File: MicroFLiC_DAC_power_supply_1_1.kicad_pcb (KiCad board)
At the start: 2 copper layers, 49.8 x 49.8 mm, 61 parts, among them P1 Socket_1x2, P2 Header_1x2, P3 Socket_2x4, U1 AP1117D50, U2 AP1117, U3 AP1117, U4 LM317, U5 LM317

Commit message: Completed part descriptions
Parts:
- U1: value AP1117D50 -> AP1117E50
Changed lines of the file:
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@@
   )
   (setup
-    (last_trace_width 0.508)
+    (last_trace_width 0.254)
     (user_trace_width 0.381)
     (user_trace_width 0.508)
@@
       (effects (font (size 1 1) (thickness 0.15)))
     )
-    (fp_text value AP1117D50 (at 0 0.762 90) (layer F.Fab) hide
-      (effects (font (size 1 1) (thickness 0.15)))
-    )
+    (fp_text value AP1117E50 (at 0 0.762 90) (layer F.Fab) hide
+      (effects (font (size 1 1) (thickness 0.15)))
+    )

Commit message: Added feedback filtering capacitors and protection diodes
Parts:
- added C21: 10u/6.3V, Capacitors_SMD:C_0805, B.Cu at (123.5, 129.0)
- added C22: 10u/6.3V, Capacitors_SMD:C_0805, B.Cu at (121.7, 137.2)
- added C23: 10u/6.3V, Capacitors_SMD:C_0805, B.Cu at (119.4, 122.4)
- added C24: 10u/6.3V, Capacitors_SMD:C_0805, B.Cu at (115.1, 111.3)
- added D6: 1N4148, Diodes_SMD:SOD-323, B.Cu at (113.3, 116.6)
- added D7: 1N4148, Diodes_SMD:SOD-323, B.Cu at (111.8, 107.2)
- added D8: 1N4148, Diodes_SMD:SOD-323, B.Cu at (111.3, 118.6)
- added D9: 1N4148, Diodes_SMD:SOD-323, B.Cu at (111.8, 110.2)
- renumbered C21 to C25, C22 to C26, C23 to C27, C24 to C28, C25 to C29
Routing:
- net /FB_D: track 4.58 -> 11.8 mm, vias 1 -> 2
- net /19V_GND: track 95.9 -> 101.8 mm, vias 1 -> 2
- net /-7.5V: track 60.2 -> 65.0 mm
- net /FB_E: track 4.44 -> 8.65 mm, vias 1 -> 2
- net /+19V: track 41.8 -> 45.2 mm, vias 1 -> 2
- net /+24_IE: track 14.5 -> 17.0 mm, vias 0 -> 1
- net /-19V: track 75.0 -> 76.4 mm
- net /+24_ID: track 13.5 -> 14.7 mm, vias 0 -> 1
- net /FB_C: track 6.29 -> 7.25 mm
- net /FB_B: vias 0 -> 1
- net /7.5V_GND: vias 2 -> 3

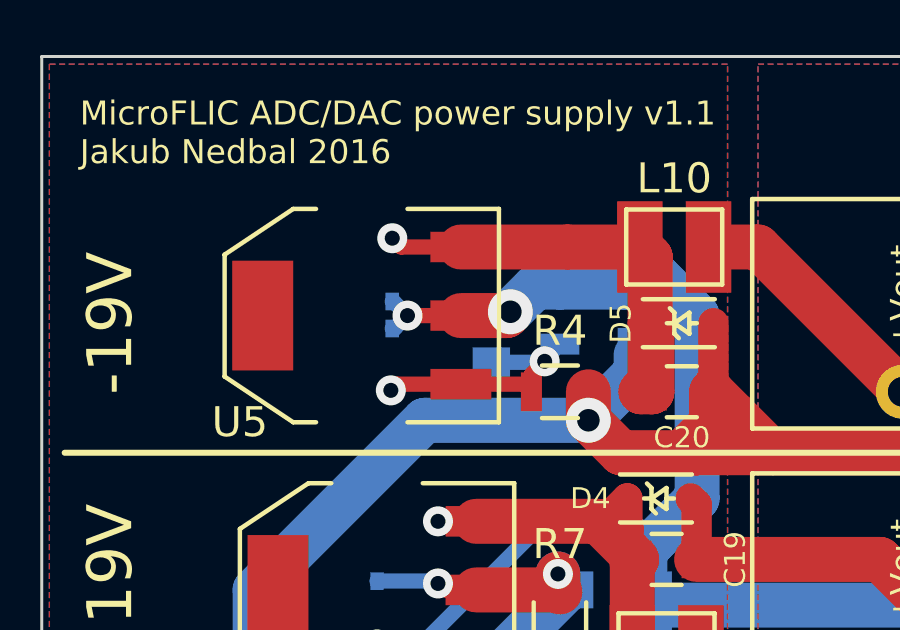
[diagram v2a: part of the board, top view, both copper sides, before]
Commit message: Fixed capacitor order code
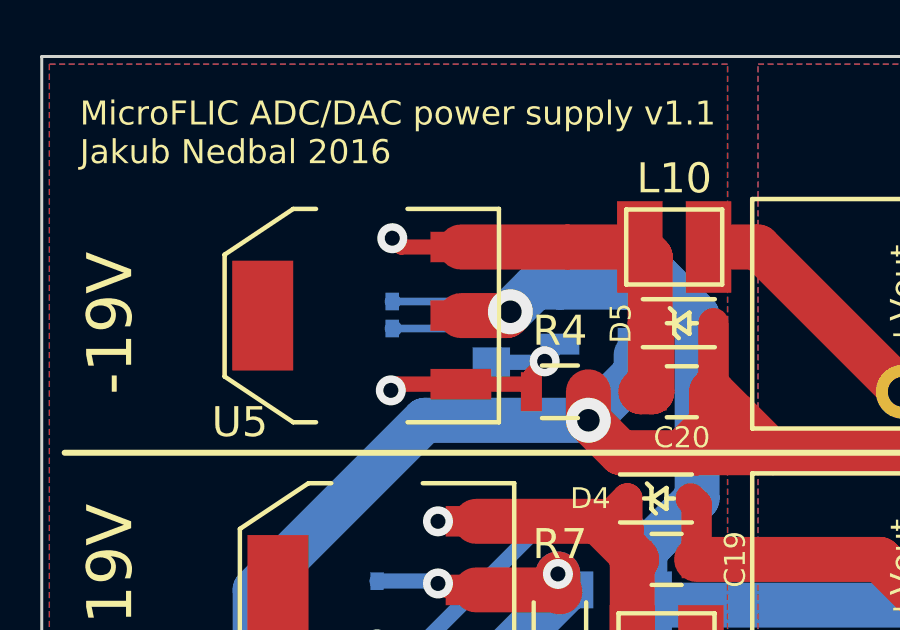
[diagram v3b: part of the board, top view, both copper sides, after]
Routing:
- net /19V_GND: track 101.8 -> 106.9 mm, vias 2 -> 1
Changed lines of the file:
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@@
     (links 130)
     (no_connects 1)
-    (area 100.025999 100.025999 149.910001 149.910001)
+    (area 99.607 100.025999 150.127 151.957)
     (thickness 1.6)
     (drawings 38)
-    (tracks 445)
+    (tracks 446)
     (zones 0)
     (modules 69)
@@
   (page A4)
   (layers
-    (0 F.Cu signal hide)
+    (0 F.Cu signal)
     (31 B.Cu signal hide)
     (32 B.Adhes user)
@@
   )
   (setup
-    (last_trace_width 0.508)
+    (last_trace_width 0.254)
     (user_trace_width 0.381)
     (user_trace_width 0.508)
@@
   (segment (start 123.952 106.426) (end 128.778 111.252) (width 1.5) (layer F.Cu) (net 25))
   (segment (start 122.303 106.426) (end 123.952 106.426) (width 1.5) (layer F.Cu) (net 25))
+  (segment (start 113.87 109.142) (end 114.427 108.585) (width 0.254) (layer B.Cu) (net 26))
+  (segment (start 114.427 108.585) (end 115.697 108.585) (width 0.254) (layer B.Cu) (net 26))
+  (segment (start 111.76 109.142) (end 113.87 109.142) (width 0.254) (layer B.Cu) (net 26))
+  (segment (start 111.76 108.243) (end 115.355 108.243) (width 0.254) (layer B.Cu) (net 26))
+  (segment (start 115.355 108.243) (end 115.697 108.585) (width 0.254) (layer B.Cu) (net 26))
   (segment (start 120.396 122.428) (end 120.396 120.462) (width 0.508) (layer B.Cu) (net 26))
   (segment (start 120.396 120.462) (end 120.33 120.396) (width 0.508) (layer B.Cu) (net 26))
   (segment (start 111.76 109.142) (end 111.838 109.142) (width 0.508) (layer B.Cu) (net 26))
-  (segment (start 111.838 109.142) (end 112.268 108.712) (width 0.508) (layer B.Cu) (net 26))
   (segment (start 111.76 108.243) (end 111.799 108.243) (width 0.508) (layer B.Cu) (net 26))
-  (segment (start 111.799 108.243) (end 112.268 108.712) (width 0.508) (layer B.Cu) (net 26))
-  (segment (start 114.046 108.712) (end 112.268 108.712) (width 0.508) (layer F.Cu) (net 26))
-  (via (at 112.268 108.712) (size 1) (drill 0.5) (layers F.Cu B.Cu) (net 26))
   (segment (start 109.22 136.906) (end 109.22 122.936) (width 1.5) (layer B.Cu) (net 26))
   (segment (start 109.22 122.936) (end 109.22 121.412) (width 1.5) (layer B.Cu) (net 26))

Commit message: Updated part descriptions
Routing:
- net /-19V: track 76.4 -> 79.6 mm
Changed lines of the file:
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@@
-(kicad_pcb (version 4) (host pcbnew 4.0.1-3.201512221402+6198~38~ubuntu14.04.1-stable)
+(kicad_pcb (version 4) (host pcbnew "(2015-12-10 BZR 6367)-product")
   (general
     (links 130)
-    (no_connects 1)
-    (area 99.607 100.025999 150.127 151.957)
+    (no_connects 0)
+    (area 100.025999 100.025999 149.910001 149.910001)
     (thickness 1.6)
     (drawings 38)
-    (tracks 446)
+    (tracks 448)
     (zones 0)
     (modules 69)
@@
   (page A4)
   (layers
-    (0 F.Cu signal)
-    (31 B.Cu signal hide)
+    (0 F.Cu signal hide)
+    (31 B.Cu signal)
     (32 B.Adhes user)
     (33 F.Adhes user)
@@
   )
   (setup
-    (last_trace_width 0.254)
+    (last_trace_width 0.508)
     (user_trace_width 0.381)
     (user_trace_width 0.508)
@@
   (segment (start 133.858 119.65) (end 135.144 118.364) (width 1.016) (layer B.Cu) (net 26))
   (segment (start 133.858 120.396) (end 133.858 119.65) (width 1.016) (layer B.Cu) (net 26))
+  (segment (start 115.062 112.268) (end 118.232 112.268) (width 0.508) (layer B.Cu) (net 27))
+  (segment (start 118.232 112.268) (end 118.298 112.202) (width 0.508) (layer B.Cu) (net 27))
   (segment (start 118.298 112.202) (end 112.842 112.202) (width 1.5) (layer B.Cu) (net 27))
   (segment (start 108.458 141.478) (end 107.188 142.748) (width 1.5) (layer B.Cu) (net 27))
